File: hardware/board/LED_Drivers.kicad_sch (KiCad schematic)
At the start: 73 parts, among them Q901 MMBT3904

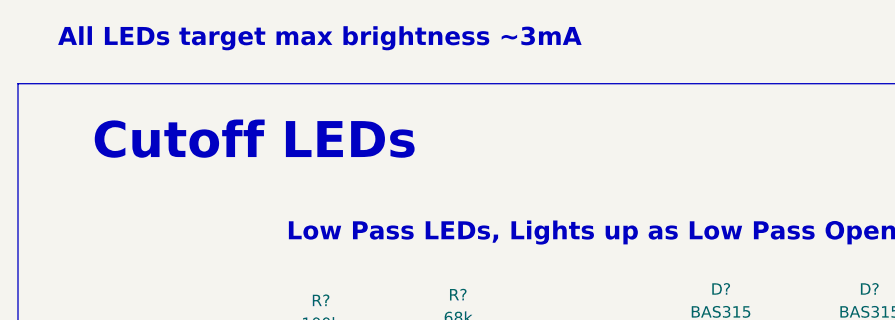
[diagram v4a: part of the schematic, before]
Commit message: Very minor schematic text change
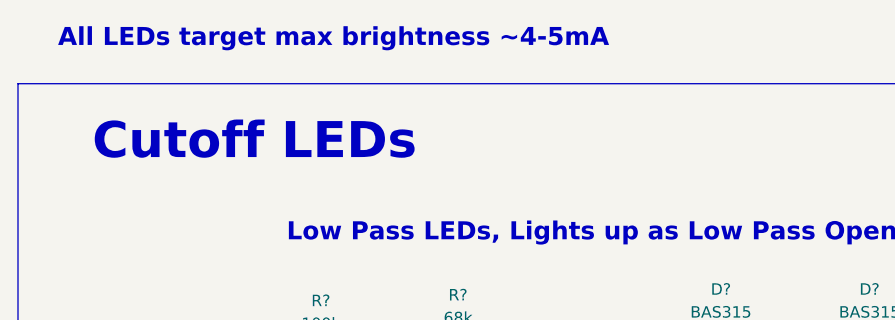
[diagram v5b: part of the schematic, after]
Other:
- note added: "All LEDs target max brightness ~4-5mA"
- note removed: "All LEDs target max brightness ~3mA"
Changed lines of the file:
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@@
     (effects (font (size 2 2) (thickness 0.4) bold) (justify left bottom))
   )
-  (text "All LEDs target max brightness ~3mA" (at 20.32 17.78 0)
+  (text "All LEDs target max brightness ~4-5mA" (at 20.32 17.78 0)
     (effects (font (size 2 2) (thickness 0.4) bold) (justify left bottom))
   )

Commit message: Lots of various small changes after reviewing the checklist.
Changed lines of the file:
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@@
   (title_block
     (title "Neptune")
-    (date "2023-09-26")
-    (rev "v0")
+    (date "2023-10-10")
+    (rev "v1")
     (company "Winterbloom")
     (comment 1 "Carson Walls")
@@
   (symbol (lib_id "Device:LED_Small_Filled") (at 249.555 115.57 90) (unit 1)
     (in_bom yes) (on_board yes) (dnp no)
-    (property "Reference" "D?" (at 252.095 113.6015 90)
+    (property "Reference" "D?" (at 252.095 114.3 90)
       (effects (font (size 1.27 1.27)) (justify right))
     )
-    (property "Value" "BLUE" (at 252.095 116.1415 90)
+    (property "Value" "BLUE" (at 252.095 116.84 90)
       (effects (font (size 1.27 1.27)) (justify right))
     )
@@
   )
   (symbol (lib_id "Device:LED_Small_Filled") (at 135.89 175.26 270) (mirror x) (unit 1)
-    (in_bom yes) (on_board yes) (dnp no)
-    (property "Reference" "D?" (at 139.7 173.99 90)
+    (in_bom yes) (on_board yes) (dnp no) (fields_autoplaced)
+    (property "Reference" "D?" (at 138.43 174.5615 90)
       (effects (font (size 1.27 1.27)) (justify left))
     )
-    (property "Value" "RED" (at 139.7 176.53 90)
+    (property "Value" "RED" (at 138.43 177.1015 90)
       (effects (font (size 1.27 1.27)) (justify left))
     )
@@
       (effects (font (size 1.27 1.27) italic) (justify left) hide)
     )
-    (property "Datasheet" "https://www.onsemi.com/pdf/datasheet/pzt3904-d.pdf" (at 133.35 162.56 0)
+    (property "Datasheet" "https://www.onsemi.com/pub/Collateral/2N3903-D.PDF" (at 133.35 162.56 0)
       (effects (font (size 1.27 1.27)) (justify left) hide)
     )
@@
       (effects (font (size 1.27 1.27)) hide)
     )
-    (property "Rating" "100mW/1%" (at 252.095 111.76 0)
+    (property "Rating" "100mW/1%" (at 252.095 111.125 0)
       (effects (font (size 1.27 1.27)) (justify left))
     )
@@
       (effects (font (size 1.27 1.27)) hide)
     )
+    (property "Notes" "" (at 85.09 60.96 0)
+      (effects (font (size 1.27 1.27)) hide)
+    )
     (pin "1")
     (pin "2")
@@
   )
   (symbol (lib_id "Device:R_US") (at 135.89 185.42 180) (unit 1)
-    (in_bom yes) (on_board yes) (dnp no)
-    (property "Reference" "R?" (at 144.145 182.88 0)
-      (effects (font (size 1.27 1.27)))
+    (in_bom yes) (on_board yes) (dnp no) (fields_autoplaced)
+    (property "Reference" "R?" (at 138.43 183.515 0)
+      (effects (font (size 1.27 1.27)) (justify right))
     )
-    (property "Value" "1k8" (at 144.145 185.42 0)
-      (effects (font (size 1.27 1.27)))
+    (property "Value" "1k8" (at 138.43 186.055 0)
+      (effects (font (size 1.27 1.27)) (justify right))
     )
     (property "Footprint" "winterbloom:R_0603_HandSolder" (at 134.874 185.166 90)
@@
       (effects (font (size 1.27 1.27)) hide)
     )
-    (property "Rating" "100mW/1%" (at 144.145 187.96 0)
-      (effects (font (size 1.27 1.27)))
+    (property "Rating" "100mW/1%" (at 138.43 188.595 0)
+      (effects (font (size 1.27 1.27)) (justify right))
     )
     (pin "1")

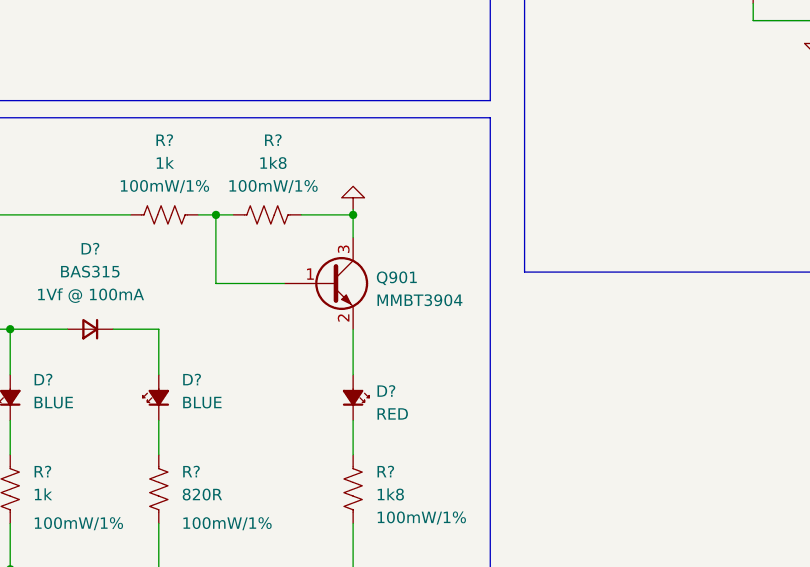
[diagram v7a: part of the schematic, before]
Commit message: Replace 3904 with 3906 transistor and swap base and collector connection
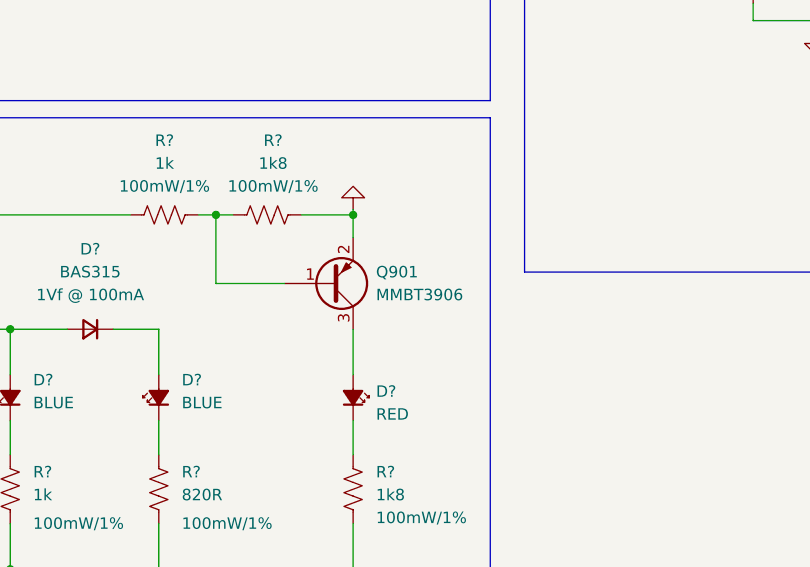
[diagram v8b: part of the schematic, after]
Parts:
- removed Q901: MMBT3904, Package_TO_SOT_SMD:SOT-23, symbol Transistor_BJT:MMBT3904
- added Q901: MMBT3906, Package_TO_SOT_SMD:SOT-23, symbol Transistor_BJT:MMBT3906
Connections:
- net GND: now also Q901.2 (E)
- net at R?.1, R?.2: now also Q901.1 (B)
- net at D?.2 (A): now also Q901.3 (C)
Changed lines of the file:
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@@
-    )
-  )
-  (symbol (lib_id "Transistor_BJT:MMBT3904") (at 133.35 162.56 0) (unit 1)
-    (in_bom yes) (on_board yes) (dnp no) (fields_autoplaced)
-    (property "Reference" "Q901" (at 138.43 161.925 0)
-      (effects (font (size 1.27 1.27)) (justify left))
-    )
-    (property "Value" "MMBT3904" (at 138.43 164.465 0)
-      (effects (font (size 1.27 1.27)) (justify left))
-    )
-    (property "Footprint" "Package_TO_SOT_SMD:SOT-23" (at 138.43 164.465 0)
-      (effects (font (size 1.27 1.27) italic) (justify left) hide)
-    )
-    (property "Datasheet" "https://www.onsemi.com/pub/Collateral/2N3903-D.PDF" (at 133.35 162.56 0)
-      (effects (font (size 1.27 1.27)) (justify left) hide)
-    )
-    (pin "1")
-    (pin "2")
-    (pin "3")
-    (instances
-      (project "mainboard"
-        (path "/960bd036-bf0c-45ea-9f41-1321756e0e5a/e3d5295b-e037-4c01-a5ad-25ec0ca0bdb3"
-          (reference "Q901") (unit 1)
-        )
-      )
     )
   )
@@
         )
       )
+    )
+  )
+  (symbol (lib_id "Transistor_BJT:MMBT3906") (at 133.35 162.56 0) (mirror x) (unit 1)
+    (in_bom yes) (on_board yes) (dnp no) (fields_autoplaced)
+    (property "Reference" "Q901" (at 138.43 161.29 0)
+      (effects (font (size 1.27 1.27)) (justify left))
+    )
+    (property "Value" "MMBT3906" (at 138.43 163.83 0)
+      (effects (font (size 1.27 1.27)) (justify left))
+    )
+    (property "Footprint" "Package_TO_SOT_SMD:SOT-23" (at 138.43 160.655 0)
+      (effects (font (size 1.27 1.27) italic) (justify left) hide)
+    )
+    (property "Datasheet" "https://www.onsemi.com/pdf/datasheet/pzt3906-d.pdf" (at 133.35 162.56 0)
+      (effects (font (size 1.27 1.27)) (justify left) hide)
+    )
+    (property "Rating" "" (at 133.35 162.56 0)
+      (effects (font (size 1.27 1.27)))
+    )
+    (property "Notes" "" (at 133.35 162.56 0)
+      (effects (font (size 1.27 1.27)) hide)
+    )
+    (property "MPN" "MMBT3906" (at 133.35 162.56 0)
+      (effects (font (size 1.27 1.27)) hide)
+    )
+    (pin "1")
+    (pin "2")
+    (pin "3")
+    (instances
+      (project "mainboard"
+        (path "/960bd036-bf0c-45ea-9f41-1321756e0e5a/e3d5295b-e037-4c01-a5ad-25ec0ca0bdb3"
+          (reference "Q901") (unit 1)
+        )
+      )
